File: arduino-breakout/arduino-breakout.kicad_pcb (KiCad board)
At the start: 2 copper layers, 90.8 x 73 mm, 26 parts, among them P0 CONN_01X06, P1 CONN_01X06, P10 CONN_01X06, P11 CONN_01X06, P12 CONN_01X06, P13 CONN_01X06, P14 CONN_01X06, P15 CONN_01X06, P16 CONN_01X06, P17 CONN_01X06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

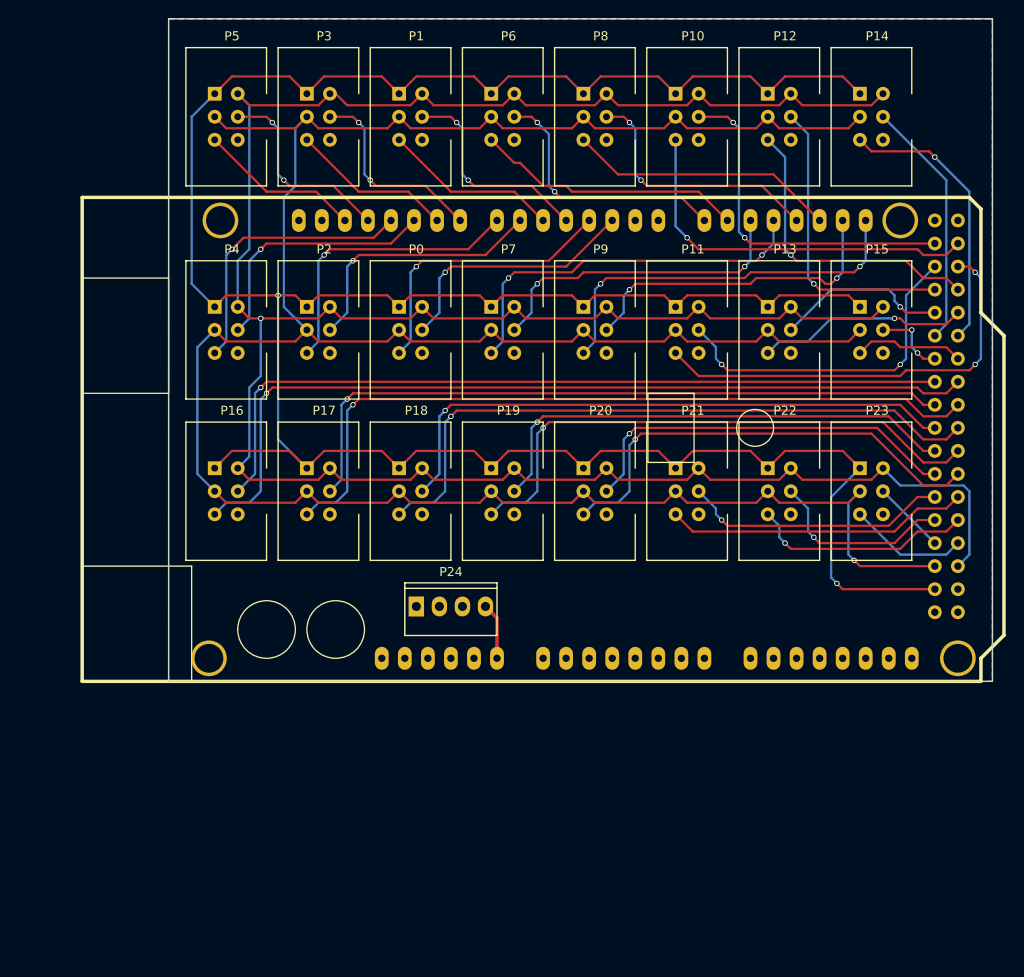
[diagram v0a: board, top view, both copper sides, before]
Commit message: Simplify Arduino mega shield library
Move the footprint to `oac-conn`.
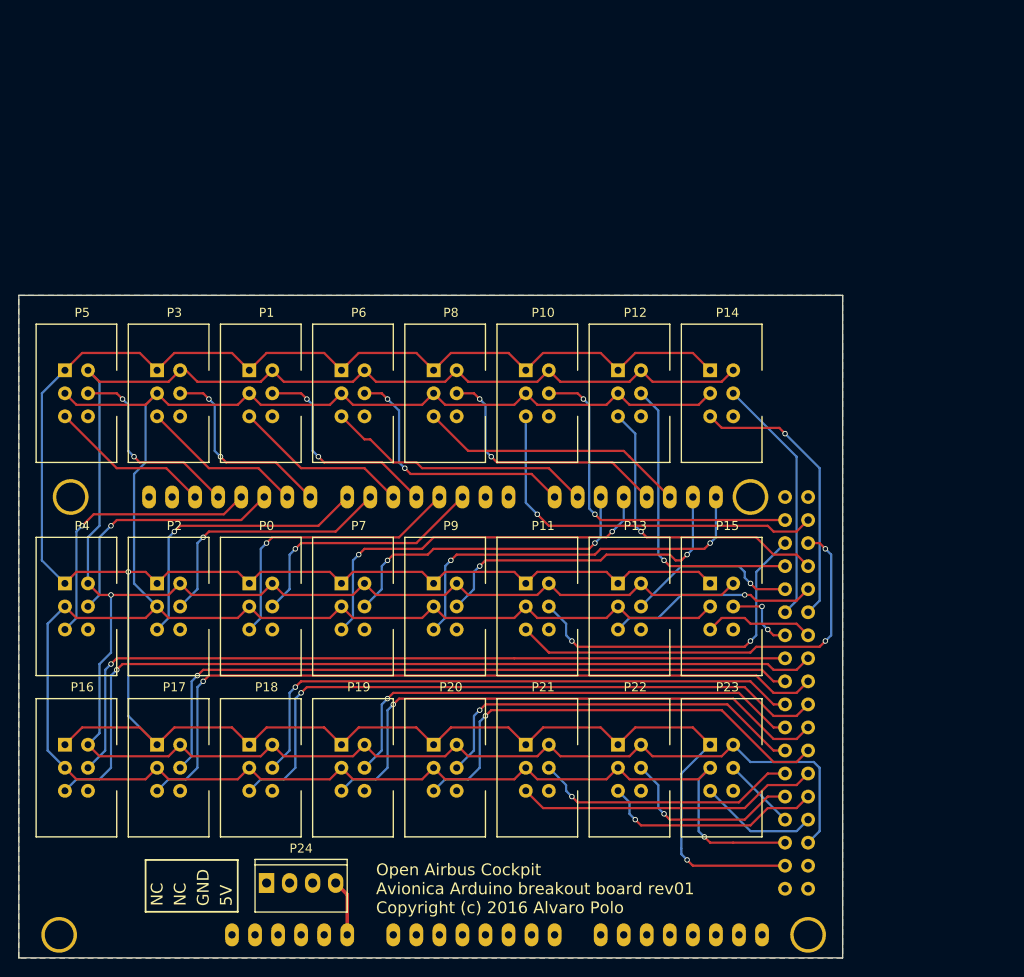
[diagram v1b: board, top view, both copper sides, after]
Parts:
- SHIELD1: footprint arduino_shields:ARDUINO_MEGA_SHIELD -> oac-conn:arduino-mega-shield
- moved P10 34.7 mm to (157.5, 61.6)
- moved P12 34.7 mm to (167.6, 61.6)
- moved P8 34.7 mm to (147.3, 61.6)
- moved P11 34.7 mm to (157.5, 85.1)
- moved P13 34.7 mm to (167.6, 85.1)
- moved P20 34.7 mm to (147.3, 102.9)
- moved P21 34.7 mm to (157.5, 102.9)
- moved P22 34.7 mm to (167.6, 102.9)
- moved P9 34.7 mm to (147.3, 85.1)
- moved P0 34.7 mm to (127.0, 85.1)
- moved P1 34.7 mm to (127.0, 61.6)
- moved P14 34.7 mm to (177.8, 61.6)
- moved P15 34.7 mm to (177.8, 85.1)
- moved P16 34.7 mm to (106.7, 102.9)
- moved P17 34.7 mm to (116.8, 102.9)
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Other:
- board text added: "5V"
- board text added: "GND"
- board text added: "NC"
- board text added: "Open Airbus Cockpit Avionica Arduino breakout board rev01 Copyright (c) 2016 Alvaro Polo"

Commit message: Move KF2510 to `oac-conn`
And reduce the dependent libraries to just that one.
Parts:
- P24: footprint ifs-connectors:KF2510-A-4P-M-TH-V -> oac-conn:kf2510-4p
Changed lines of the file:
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@@
     (pad_drill 0.762)
     (pad_to_mask_clearance 0.2)
-    (aux_axis_origin 100.33 127.635)
+    (aux_axis_origin 120.65 133.35)
     (visible_elements FFFFFF7F)
     (pcbplotparams
@@
       (net 6 GND))
   )
-  (module ifs-connectors:KF2510-A-4P-M-TH-V (layer F.Cu)
-    (at 132.715 118.11)
-    (fp_text reference P24 (at 0 -3.81) (layer F.SilkS)
-      (effects (font (size 1 1) (thickness 0.15)))
-    )
-    (fp_text value CONN_01X04 (at 0 5.08) (layer F.Fab)
-      (effects (font (size 1 1) (thickness 0.15)))
-    )
-    (fp_line (start -5.08 -2) (end 5.08 -2) (layer F.SilkS) (width 0.15))
-    (fp_line (start -5.33 -2.85) (end 5.33 -2.85) (layer F.CrtYd) (width 0.05))
-    (fp_line (start 5.33 -2.85) (end 5.33 3.45) (layer F.CrtYd) (width 0.05))
-    (fp_line (start 5.33 3.45) (end -5.33 3.45) (layer F.CrtYd) (width 0.05))
-    (fp_line (start -5.33 3.45) (end -5.33 -2.85) (layer F.CrtYd) (width 0.05))
-    (fp_line (start -5.08 -2.6) (end 5.08 -2.6) (layer F.SilkS) (width 0.15))
-    (fp_line (start 5.08 -2.6) (end 5.08 3.2) (layer F.SilkS) (width 0.15))
-    (fp_line (start 5.08 3.2) (end -5.08 3.2) (layer F.SilkS) (width 0.15))
-    (fp_line (start -5.08 3.2) (end -5.08 -2.6) (layer F.SilkS) (width 0.15))
-    (pad 1 thru_hole rect (at -3.81 0) (size 1.7 2.2) (drill 1) (layers *.Cu *.Mask F.SilkS)
-      (net 79 "Net-(P24-Pad1)"))
-    (pad 2 thru_hole oval (at -1.27 0) (size 1.7 2.2) (drill 1) (layers *.Cu *.Mask F.SilkS)
-      (net 80 "Net-(P24-Pad2)"))
-    (pad 3 thru_hole oval (at 1.27 0) (size 1.7 2.2) (drill 1) (layers *.Cu *.Mask F.SilkS)
-      (net 6 GND))
-    (pad 4 thru_hole oval (at 3.81 0) (size 1.7 2.2) (drill 1) (layers *.Cu *.Mask F.SilkS)
-      (net 53 VCC))
-    (model 3D/Connector/KF2510-A-4P-M-TH-V.wrl
-      (at (xyz 0 0 0.0025))
-      (scale (xyz 0.393701 0.393701 0.393701))
-      (rotate (xyz 0 0 0))
-    )
-  )
   (module oac-conn:arduino-mega-shield (layer F.Cu)
     (at 92.075 126.365)
@@
       (rotate (xyz 0 0 0))
     )
+  )
+  (module oac-conn:kf2510-4p (layer F.Cu)
+    (at 132.715 118.11)
+    (fp_text reference P24 (at 0 -3.81) (layer F.SilkS)
+      (effects (font (size 1 1) (thickness 0.15)))
+    )
+    (fp_text value CONN_01X04 (at 0 5.08) (layer F.Fab)
+      (effects (font (size 1 1) (thickness 0.15)))
+    )
+    (fp_line (start -5.08 -2) (end 5.08 -2) (layer F.SilkS) (width 0.15))
+    (fp_line (start -5.33 -2.85) (end 5.33 -2.85) (layer F.CrtYd) (width 0.05))
+    (fp_line (start 5.33 -2.85) (end 5.33 3.45) (layer F.CrtYd) (width 0.05))
+    (fp_line (start 5.33 3.45) (end -5.33 3.45) (layer F.CrtYd) (width 0.05))
+    (fp_line (start -5.33 3.45) (end -5.33 -2.85) (layer F.CrtYd) (width 0.05))
+    (fp_line (start -5.08 -2.6) (end 5.08 -2.6) (layer F.SilkS) (width 0.15))
+    (fp_line (start 5.08 -2.6) (end 5.08 3.2) (layer F.SilkS) (width 0.15))
+    (fp_line (start 5.08 3.2) (end -5.08 3.2) (layer F.SilkS) (width 0.15))
+    (fp_line (start -5.08 3.2) (end -5.08 -2.6) (layer F.SilkS) (width 0.15))
+    (pad 1 thru_hole rect (at -3.81 0) (size 1.7 2.2) (drill 1) (layers *.Cu *.Mask F.SilkS)
+      (net 79 "Net-(P24-Pad1)"))
+    (pad 2 thru_hole oval (at -1.27 0) (size 1.7 2.2) (drill 1) (layers *.Cu *.Mask F.SilkS)
+      (net 80 "Net-(P24-Pad2)"))
+    (pad 3 thru_hole oval (at 1.27 0) (size 1.7 2.2) (drill 1) (layers *.Cu *.Mask F.SilkS)
+      (net 6 GND))
+    (pad 4 thru_hole oval (at 3.81 0) (size 1.7 2.2) (drill 1) (layers *.Cu *.Mask F.SilkS)
+      (net 53 VCC))
+    (model 3D/Connector/KF2510-A-4P-M-TH-V.wrl
+      (at (xyz 0 0 0.0025))
+      (scale (xyz 0.393701 0.393701 0.393701))
+      (rotate (xyz 0 0 0))
+    )
